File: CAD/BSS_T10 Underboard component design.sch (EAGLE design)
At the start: 10 parts

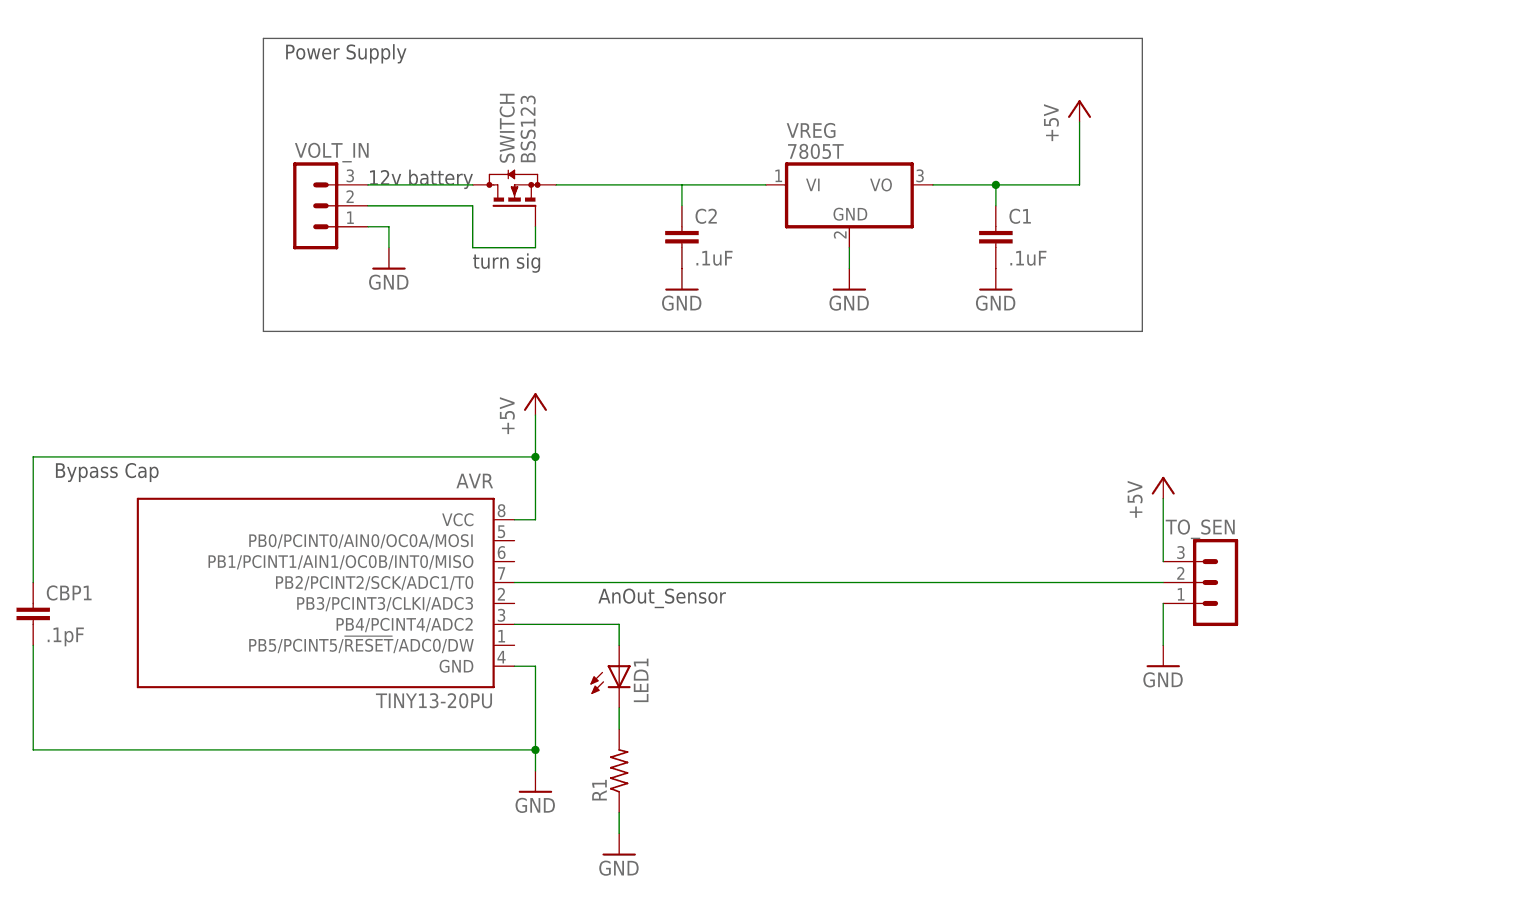
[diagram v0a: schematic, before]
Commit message: Board Layout
Uploaded board layout with components on both sides of board
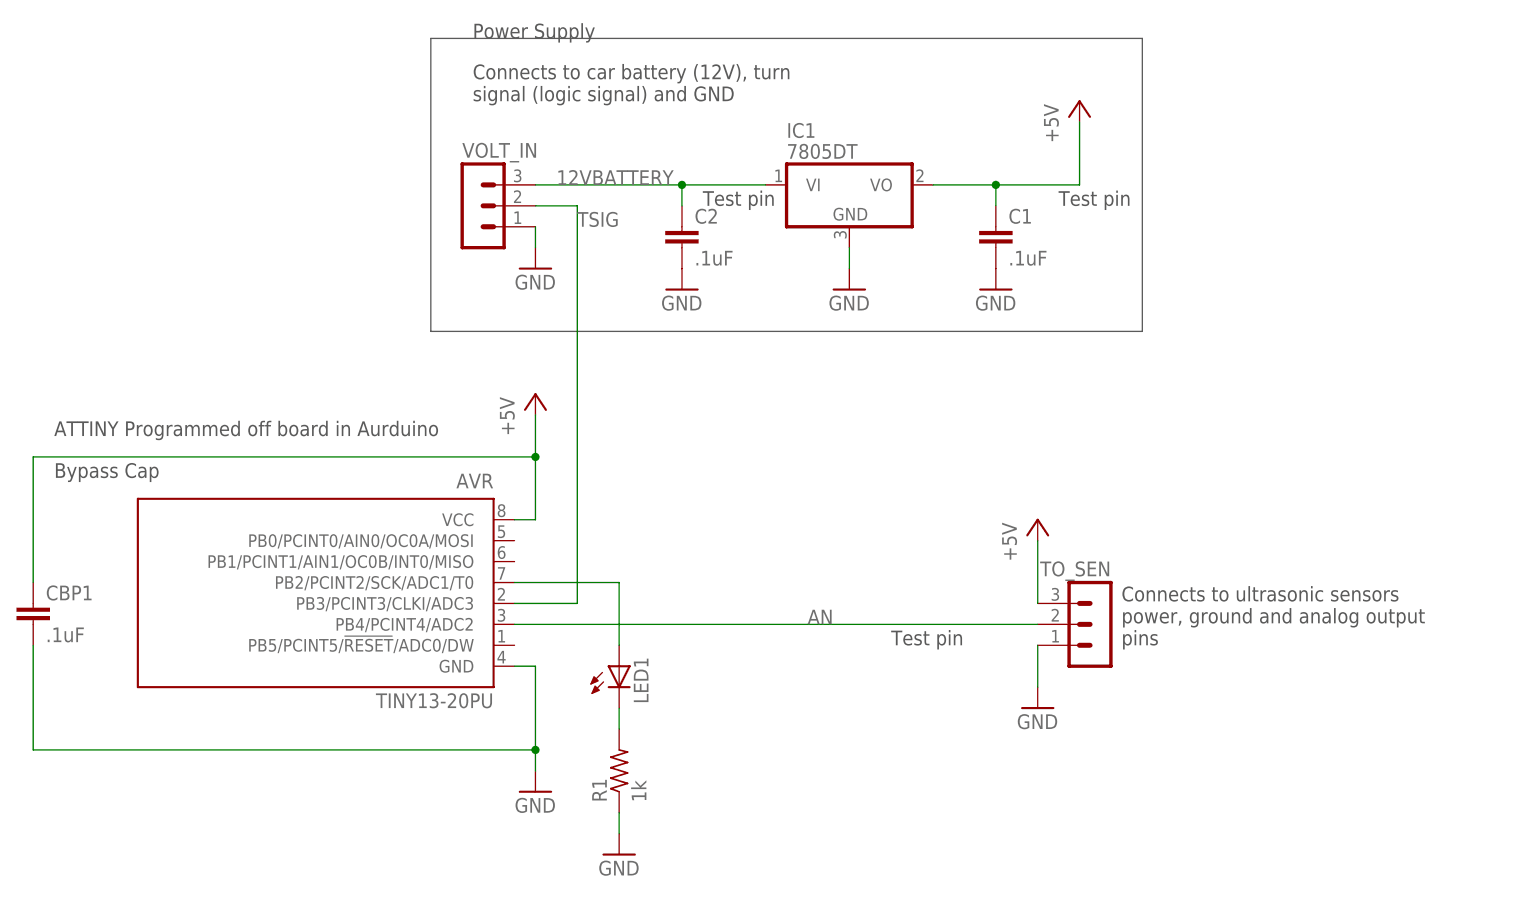
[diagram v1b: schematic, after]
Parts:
- removed SWITCH: BSS123, transistor-small-signal:BSS123
- removed VREG: 7805T, linear:7805T
- added IC1: 7805DT, linear:7805DT
- CBP1: value .1pF -> .1uF
- R1: value (none) -> 1k
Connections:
- net N$3 renamed RLED
- removed net BATTERY: SWITCH.D, VOLT_IN.3
- removed net N$1: SWITCH.S, VREG.VI
- removed net N$2: C2.1
- removed net N$8: AVR.PB2/PCINT2/SCK/ADC1/T0, TO_SEN.2
- new net 12VBATTERY: C2.1, IC1.VI, VOLT_IN.3
- new net AN: AVR.PB4/PCINT4/ADC2, TO_SEN.2
- net +5V: now also IC1.VO; no longer VREG.VO
- net GND: now also IC1.GND; no longer VREG.GND
- net N$4: now also AVR.PB2/PCINT2/SCK/ADC1/T0; no longer AVR.PB4/PCINT4/ADC2
- net TSIG: now also AVR.PB3/PCINT3/CLKI/ADC3; no longer SWITCH.G
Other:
- note added: "ATTINY Programmed off board in Aurduino"
- note added: "Connects to car battery (12V), turn signal (logic signal) and GND"
- note added: "Connects to ultrasonic sensors power, ground and analog output pins"
- note added: "Test pin"
- note removed: "12v battery"
- note removed: "AnOut_Sensor"
- note removed: "turn sig"
- moved on the sheet: TO_SEN, VOLT_IN
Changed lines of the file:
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@@
 <?xml version="1.0" encoding="utf-8"?>
 <!DOCTYPE eagle SYSTEM "eagle.dtd">
-<eagle version="7.4.0">
+<eagle version="6.5.0">
 <drawing>
 <settings>
@@
 <setting verticaltext="up"/>
 </settings>
-<grid distance="0.1" unitdist="inch" unit="inch" style="lines" multiple="1" display="yes" altdistance="0.01" altunitdist="inch" altunit="inch"/>
+<grid distance="0.1" unitdist="inch" unit="inch" style="lines" multiple="1" display="no" altdistance="0.01" altunitdist="inch" altunit="inch"/>
 <layers>
 <layer number="1" name="Top" color="4" fill="1" visible="no" active="no"/>
@@
 <part name="P+2" library="supply1" deviceset="+5V" device=""/>
 <part name="GND1" library="supply1" deviceset="GND" device=""/>
-<part name="CBP1" library="rcl" deviceset="C-EU" device="C0805" value=".1pF"/>
+<part name="CBP1" library="rcl" deviceset="C-EU" device="C0805" value=".1uF"/>
 <part name="C1" library="rcl" deviceset="C-EU" device="C0805" value=".1uF"/>
 <part name="C2" library="rcl" deviceset="C-EU" device="C0805" value=".1uF"/>
@@
 <part name="GND5" library="supply1" deviceset="GND" device=""/>
 <part name="P+3" library="supply1" deviceset="+5V" device=""/>
-<part name="R1" library="rcl" deviceset="R-US_" device="R0805"/>
-<part name="VREG" library="linear" deviceset="78*" device="T" technology="05"/>
+<part name="R1" library="rcl" deviceset="R-US_" device="R0805" value="1k"/>
 <part name="GND6" library="supply1" deviceset="GND" device=""/>
-<part name="SWITCH" library="transistor-small-signal" deviceset="BSS123" device=""/>
 <part name="LED1" library="led" deviceset="LED" device="5MM"/>
 <part name="VOLT_IN" library="con-lstb" deviceset="MA03-1" device=""/>
-<part name="GND7" library="supply1" deviceset="GND" device=""/>
 <part name="TO_SEN" library="con-lstb" deviceset="MA03-1" device=""/>
 <part name="GND2" library="supply1" deviceset="GND" device=""/>
+<part name="FRAME2" library="frames" deviceset="DINA5_L" device=""/>
+<part name="IC1" library="linear" deviceset="78*" device="DT" technology="05"/>
 <part name="P+1" library="supply1" deviceset="+5V" device=""/>
-<part name="FRAME2" library="frames" deviceset="DINA5_L" device=""/>
+<part name="GND7" library="supply1" deviceset="GND" device=""/>
 </parts>
 <sheets>
 <sheet>
 <plain>
-<text x="45.72" y="27.94" size="1.778" layer="97">AnOut_Sensor</text>
-<text x="17.78" y="78.74" size="1.778" layer="97">12v battery</text>
-<text x="30.48" y="68.58" size="1.778" layer="97">turn sig</text>
 <text x="-20.32" y="43.18" size="1.778" layer="97">Bypass Cap</text>
-<wire x1="5.08" y1="60.96" x2="111.76" y2="60.96" width="0.1524" layer="97"/>
+<wire x1="25.4" y1="60.96" x2="111.76" y2="60.96" width="0.1524" layer="97"/>
 <wire x1="111.76" y1="60.96" x2="111.76" y2="96.52" width="0.1524" layer="97"/>
-<wire x1="111.76" y1="96.52" x2="5.08" y2="96.52" width="0.1524" layer="97"/>
-<wire x1="5.08" y1="96.52" x2="5.08" y2="60.96" width="0.1524" layer="97"/>
-<text x="7.62" y="93.98" size="1.778" layer="97">Power Supply</text>
+<wire x1="111.76" y1="96.52" x2="25.4" y2="96.52" width="0.1524" layer="97"/>
+<wire x1="25.4" y1="96.52" x2="25.4" y2="60.96" width="0.1524" layer="97"/>
+<text x="30.48" y="96.52" size="1.778" layer="97">Power Supply</text>
+<text x="109.22" y="22.86" size="1.778" layer="97">Connects to ultrasonic sensors
+power, ground and analog output
+pins</text>
+<text x="30.48" y="88.9" size="1.778" layer="97">Connects to car battery (12V), turn
+signal (logic signal) and GND</text>
+<text x="-20.32" y="48.26" size="1.778" layer="97">ATTINY Programmed off board in Aurduino</text>
+<text x="81.28" y="22.86" size="1.778" layer="97">Test pin</text>
+<text x="101.6" y="76.2" size="1.778" layer="97">Test pin</text>
+<text x="58.42" y="76.2" size="1.778" layer="97">Test pin</text>
 </plain>
 <instances>
@@
 <instance part="P+3" gate="1" x="104.14" y="88.9"/>
 <instance part="R1" gate="G$1" x="48.26" y="7.62" rot="R90"/>
-<instance part="VREG" gate="A1" x="76.2" y="78.74"/>
 <instance part="GND6" gate="1" x="48.26" y="-2.54"/>
-<instance part="SWITCH" gate="G$1" x="35.56" y="78.74" rot="R90"/>
 <instance part="LED1" gate="G$1" x="48.26" y="20.32"/>
-<instance part="VOLT_IN" gate="G$1" x="10.16" y="76.2"/>
-<instance part="GND7" gate="1" x="20.32" y="68.58"/>
-<instance part="TO_SEN" gate="G$1" x="121.92" y="30.48" rot="MR0"/>
-<instance part="GND2" gate="1" x="114.3" y="20.32"/>
-<instance part="P+1" gate="1" x="114.3" y="43.18"/>
+<instance part="VOLT_IN" gate="G$1" x="30.48" y="76.2"/>
+<instance part="TO_SEN" gate="G$1" x="106.68" y="25.4" rot="MR0"/>
+<instance part="GND2" gate="1" x="99.06" y="15.24"/>
 <instance part="FRAME2" gate="G$1" x="-33.02" y="-25.4"/>
+<instance part="IC1" gate="A1" x="76.2" y="78.74"/>
+<instance part="P+1" gate="1" x="99.06" y="38.1"/>
+<instance part="GND7" gate="1" x="38.1" y="68.58"/>
 </instances>
 <busses>
@@
 <wire x1="104.14" y1="78.74" x2="93.98" y2="78.74" width="0.1524" layer="91"/>
 <junction x="93.98" y="78.74"/>
-<pinref part="VREG" gate="A1" pin="VO"/>
+<pinref part="IC1" gate="A1" pin="VO"/>
 </segment>
 <segment>
 <pinref part="TO_SEN" gate="G$1" pin="3"/>
-<wire x1="114.3" y1="33.02" x2="114.3" y2="40.64" width="0.1524" layer="91"/>
+<wire x1="99.06" y1="27.94" x2="99.06" y2="35.56" width="0.1524" layer="91"/>
 <pinref part="P+1" gate="1" pin="+5V"/>
 </segment>
@@
 <pinref part="GND5" gate="1" pin="GND"/>
 <wire x1="76.2" y1="68.58" x2="76.2" y2="71.12" width="0.1524" layer="91"/>
-<pinref part="VREG" gate="A1" pin="GND"/>
+<pinref part="IC1" gate="A1" pin="GND"/>
 </segment>
 <segment>
@@
 </segment>
 <segment>
+<pinref part="TO_SEN" gate="G$1" pin="1"/>
+<wire x1="99.06" y1="22.86" x2="99.06" y2="17.78" width="0.1524" layer="91"/>
+<pinref part="GND2" gate="1" pin="GND"/>
+</segment>
+<segment>
 <pinref part="VOLT_IN" gate="G$1" pin="1"/>
-<wire x1="17.78" y1="73.66" x2="20.32" y2="73.66" width="0.1524" layer="91"/>
-<wire x1="20.32" y1="73.66" x2="20.32" y2="71.12" width="0.1524" layer="91"/>
+<wire x1="38.1" y1="73.66" x2="38.1" y2="71.12" width="0.1524" layer="91"/>
 <pinref part="GND7" gate="1" pin="GND"/>
 </segment>
-<segment>
-<pinref part="TO_SEN" gate="G$1" pin="1"/>
-<wire x1="114.3" y1="27.94" x2="114.3" y2="22.86" width="0.1524" layer="91"/>
-<pinref part="GND2" gate="1" pin="GND"/>
-</segment>
-</net>
-<net name="N$1" class="0">
-<segment>
-<pinref part="VREG" gate="A1" pin="VI"/>
-<pinref part="SWITCH" gate="G$1" pin="S"/>
-<wire x1="40.64" y1="78.74" x2="66.04" y2="78.74" width="0.1524" layer="91"/>
-</segment>
-</net>
-<net name="N$4" class="0">
-<segment>
-<pinref part="AVR" gate="G$1" pin="PB4/PCINT4/ADC2"/>
-<wire x1="48.26" y1="25.4" x2="35.56" y2="25.4" width="0.1524" layer="91"/>
-<wire x1="48.26" y1="22.86" x2="48.26" y2="25.4" width="0.1524" layer="91"/>
-<pinref part="LED1" gate="G$1" pin="A"/>
-</segment>
 </net>
 <net name="TSIG" class="0">
 <segment>
-<pinref part="SWITCH" gate="G$1" pin="G"/>
-<wire x1="38.1" y1="73.66" x2="38.1" y2="71.12" width="0.1524" layer="91"/>
-<wire x1="30.48" y1="76.2" x2="30.48" y2="71.12" width="0.1524" layer="91"/>
-<wire x1="30.48" y1="71.12" x2="38.1" y2="71.12" width="0.1524" layer="91"/>
+<wire x1="43.18" y1="76.2" x2="43.18" y2="27.94" width="0.1524" layer="91"/>
 <pinref part="VOLT_IN" gate="G$1" pin="2"/>
-<wire x1="17.78" y1="76.2" x2="30.48" y2="76.2" width="0.1524" layer="91"/>
-</segment>
-</net>
-<net name="N$3" class="0">
+<wire x1="43.18" y1="76.2" x2="38.1" y2="76.2" width="0.1524" layer="91"/>
+<label x="43.18" y="73.66" size="1.778" layer="95"/>
+<pinref part="AVR" gate="G$1" pin="PB3/PCINT3/CLKI/ADC3"/>
+<wire x1="43.18" y1="27.94" x2="35.56" y2="27.94" width="0.1524" layer="91"/>
+</segment>
+</net>
+<net name="RLED" class="0">
 <segment>
 <pinref part="R1" gate="G$1" pin="2"/>
@@
 </segment>
 </net>
-<net name="BATTERY" class="0">
-<segment>
-<pinref part="VOLT_IN" gate="G$1" pin="3"/>
-<pinref part="SWITCH" gate="G$1" pin="D"/>
-<wire x1="17.78" y1="78.74" x2="30.48" y2="78.74" width="0.1524" layer="91"/>
-</segment>
-</net>
-<net name="N$8" class="0">
-<segment>
-<pinref part="TO_SEN" gate="G$1" pin="2"/>
-<pinref part="AVR" gate="G$1" pin="PB2/PCINT2/SCK/ADC1/T0"/>
-<wire x1="114.3" y1="30.48" x2="35.56" y2="30.48" width="0.1524" layer="91"/>
-</segment>
-</net>
-<net name="N$2" class="0">
-<segment>
+<net name="12VBATTERY" class="0">
+<segment>
+<wire x1="66.04" y1="78.74" x2="55.88" y2="78.74" width="0.1524" layer="91"/>
 <pinref part="C2" gate="G$1" pin="1"/>
 <wire x1="55.88" y1="76.2" x2="55.88" y2="78.74" width="0.1524" layer="91"/>
+<pinref part="IC1" gate="A1" pin="VI"/>
+<pinref part="VOLT_IN" gate="G$1" pin="3"/>
+<wire x1="38.1" y1="78.74" x2="55.88" y2="78.74" width="0.1524" layer="91"/>
+<junction x="55.88" y="78.74"/>
+<label x="40.64" y="78.74" size="1.778" layer="95"/>
+</segment>
+</net>
+<net name="AN" class="0">
+<segment>
+<pinref part="AVR" gate="G$1" pin="PB4/PCINT4/ADC2"/>
+<pinref part="TO_SEN" gate="G$1" pin="2"/>
+<wire x1="35.56" y1="25.4" x2="99.06" y2="25.4" width="0.1524" layer="91"/>
+<label x="71.12" y="25.4" size="1.778" layer="95"/>
+</segment>
+</net>
+<net name="N$4" class="0">
+<segment>
+<pinref part="LED1" gate="G$1" pin="A"/>
+<wire x1="48.26" y1="22.86" x2="48.26" y2="30.48" width="0.1524" layer="91"/>
+<pinref part="AVR" gate="G$1" pin="PB2/PCINT2/SCK/ADC1/T0"/>
+<wire x1="48.26" y1="30.48" x2="35.56" y2="30.48" width="0.1524" layer="91"/>
 </segment>
 </net>
@@
 </sheet>
 </sheets>
+<errors>
+</errors>
 </schematic>
 </drawing>
+<compatibility>
+<note version="6.3" minversion="6.2.2" severity="warning">
+Since Version 6.2.2 text objects can contain more than one line,
+which will not be processed correctly with this version.
+</note>
+</compatibility>
 </eagle>
